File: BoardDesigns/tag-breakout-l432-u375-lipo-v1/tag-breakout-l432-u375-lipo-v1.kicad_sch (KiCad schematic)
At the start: 29 parts, among them J1 Conn_01x04_Female, J102 Conn_02x05_Odd_Even, J104 USB_B_Mini, J2 Conn_01x02_Male, J5 Conn_01x02_Male, U1 XC6206, U10 AP2112K-1.8, U105 Tactile Switch, U2 SiP32432DR3, U5 stm32l432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

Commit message: update design
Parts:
- added C102, C103, C109, C110, C111: 0.1uF, Capacitor_SMD:C_0402_1005Metric, symbol Device:C
- added FID1, FID2, FID3: Fiducial, Fiducial:Fiducial_0.5mm_Mask1mm, symbol Mechanical:Fiducial
- added U4: USBLC6-2P6, Package_TO_SOT_SMD:SOT-666, symbol Power_Protection:USBLC6-2P6
- D1: footprint LED_SMD:LED_0603_1608Metric -> LED_SMD:LED_0805_2012Metric; LCSC C5123548 -> C2297; MFN Silverlight -> Hubei KENTO Elec; MPN P0603P1N46G12 -> KT-0805G; Macrofab MF-LED-0603-GREEN -> (none)
- R1: value 510 -> 100; LCSC C25123 -> C25076; MPN 0402WGF5100TCE -> 0402WGF1000TCE
- R107: value 510 -> 200; LCSC C25123 -> C25087; MFN Uniroyal Elec -> Uniroyal Elec.; MPN 0402WGF5100TCE -> 0402WGF2000TCE
- U2: symbol Power_Management:SiP32432DR3 -> libraries:SiP32432DR3
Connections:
- net +1V8: now also C103.1, C109.1
- net +3V3: now also C110.1, C111.1
- net GND: now also C102.2, C103.2, C109.2, C110.2, C111.2, U4.2 (GND)
- net USB_DM: now also U4.3 (I/O2); no longer J104.2 (D-)
- net USB_DP: now also U4.1 (I/O1); no longer J104.3 (D+)
- net VUSB: now also C102.1, U4.5 (VBUS)
- net EXT_PWR: no longer names the net of J1.3 (Pin_3)
- new net DM: J104.2 (D-), U4.4 (I/O2)
- new net DP: J104.3 (D+), U4.6 (I/O1)
- no-connect marks 3 -> 17

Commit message: check in 2 layer board
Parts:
- removed FID1, FID2, FID3: Fiducial, Fiducial:Fiducial_0.5mm_Mask1mm, symbol Mechanical:Fiducial
- removed J5: Conn_01x02_Male, Connector_PinHeader_2.54mm:PinHeader_1x02_P2.54mm_Vertical, symbol Connector_Generic:Conn_01x02
- added R2: 100, Resistor_SMD:R_0402_1005Metric, symbol Device:R
- added TP1, TP2: TestPoint, TestPoint:TestPoint_Pad_D2.5mm, symbol Connector:TestPoint
- R106: value 200 -> 100; LCSC C25087 -> C25076; MFN Uniroyal Elec. -> Uniroyal Elec; MPN 0402WGF2000TCE -> 0402WGF1000TCE
- U10: LCSC C176944 -> C22365428; MFN Diodes -> MSKSEMI; MPN AP2112K-1.8TRG1 -> AP2112K-1.8TRG1(MS)
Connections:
- net at U5.26 (PB3), U7.3 (A): now also TP2.1
- net at U5.27 (PB4), U8.3 (A): now also R2.2, TP1.1; no longer U5.28 (PB5)
- new net: R2.1, U5.28 (PB5)
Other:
- note added: "5 Pin package but pin 4 is defined as NC in datasheet"
- note removed: "Diodes don't have footprints yet"
- title: Tag Breakout Board with stm32l432k -> Tag Breakout Board with stm32l432k and stm32u375

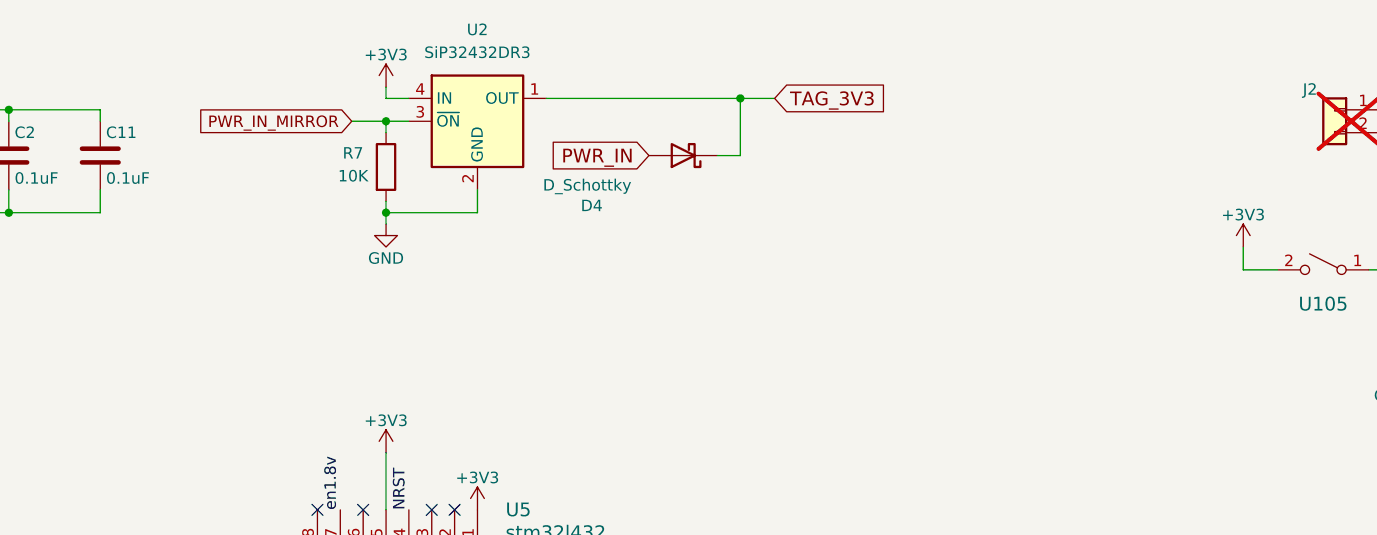
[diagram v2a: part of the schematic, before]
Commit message: Update IMU breakout and bittag base designs
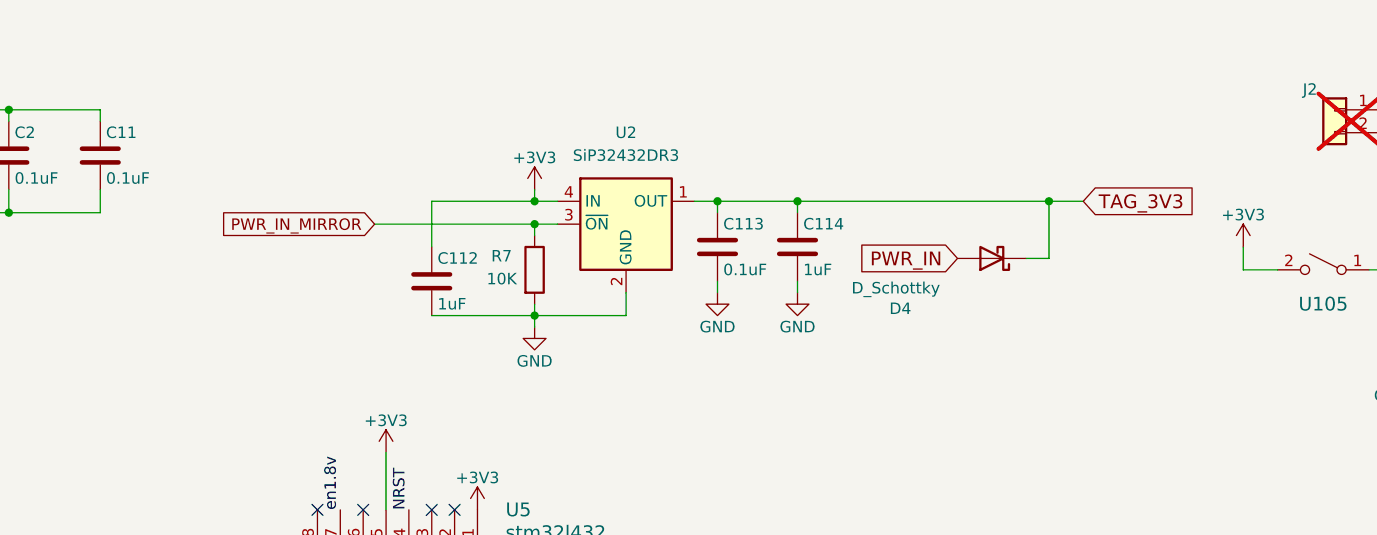
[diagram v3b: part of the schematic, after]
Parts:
- added C112, C114: 1uF, Capacitor_SMD:C_0402_1005Metric, symbol Device:C
- added C113: 0.1uF, Capacitor_SMD:C_0402_1005Metric, symbol Device:C
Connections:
- net +3V3: now also C112.1
- net GND: now also C112.2, C113.2, C114.2
- net TAG_3V3: now also C113.1, C114.1
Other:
- moved on the sheet: D4, R7, U2
